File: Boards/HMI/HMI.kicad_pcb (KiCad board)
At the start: 2 copper layers, 250 x 150 mm, 177 parts, among them IC1 ISO1042BDWVR, IC6 MCP2515-e_ST, J1 1987724, J10 5442251, J11 5442251, J12 5442251, J13 5442251, J14 5442251, J15 5442251, J16 5442251, J17 5442251, J18 5442251, J19 5442251, J2 1987724, J20 5442251, J21 5442251, J22 5442251, J23 5442251, J24 5442251, J25 5442251, J26 5442251, J27 5442251, J28 5442251, J29 5442251, J3 5442251, J30 5442251, J31 5442251, J32 5442251, J33 5442251, J34 5442251, J35 5442251, J36 5442251, J37 5442251, J38 5442251, J39 5442251, J4 5442251, J40 5442251, J41 5442251, J42 5442251, J43 5442251, J44 5442251, J45 5442251, J46 5442251, J47 5442251, J48 5442251, J49 5442251, J5 5442251, J50 5442251, J51 5442251, J52 5442251, J53 5442251, J54 5442251, J55 5442251, J56 5442251, J57 5442251, J58 5442251, J6 5442251, J7 5442251, J8 5442251, J9 5442251, Q1 SSM3K361R,LF, Q10 SSM3K361R,LF, Q11 SSM3K361R,LF, Q12 SSM3K361R,LF, Q13 SSM3K361R,LF, Q14 SSM3K361R,LF, Q15 SSM3K361R,LF, Q16 SSM3K361R,LF, Q17 SSM3K361R,LF, Q18 SSM3K361R,LF, Q19 SSM3K361R,LF, Q2 SSM3K361R,LF, Q20 SSM3K361R,LF, Q21 SSM3K361R,LF, Q22 SSM3K361R,LF, Q23 SSM3K361R,LF, Q24 SSM3K361R,LF, Q3 SSM3K361R,LF, Q4 SSM3K361R,LF, Q5 SSM3K361R,LF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

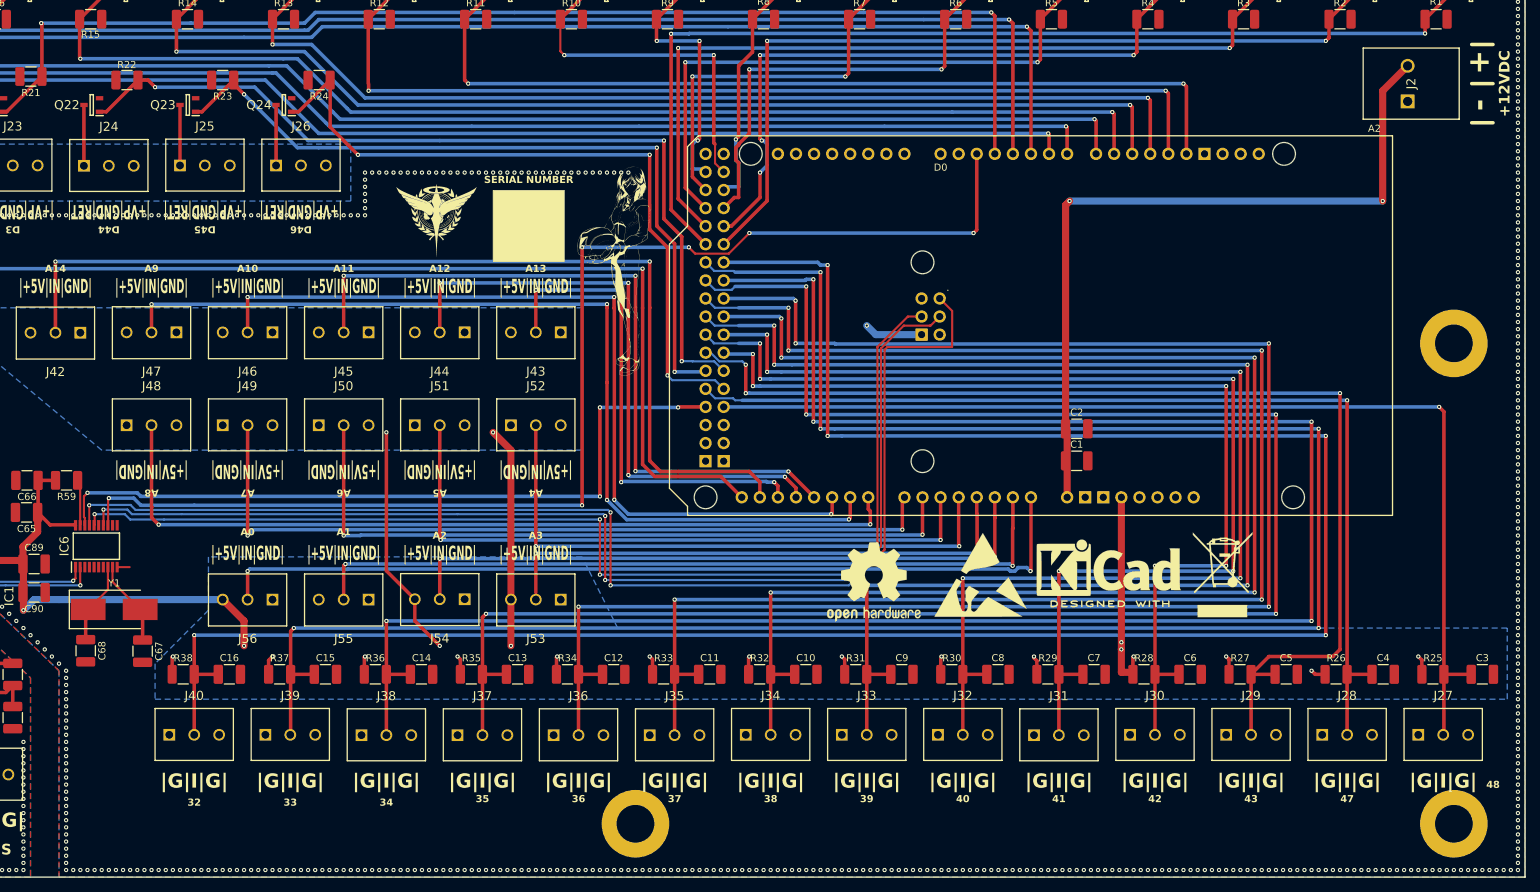
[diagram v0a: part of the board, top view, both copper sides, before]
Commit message: Update Gate Driver to use non NDA BS Chip
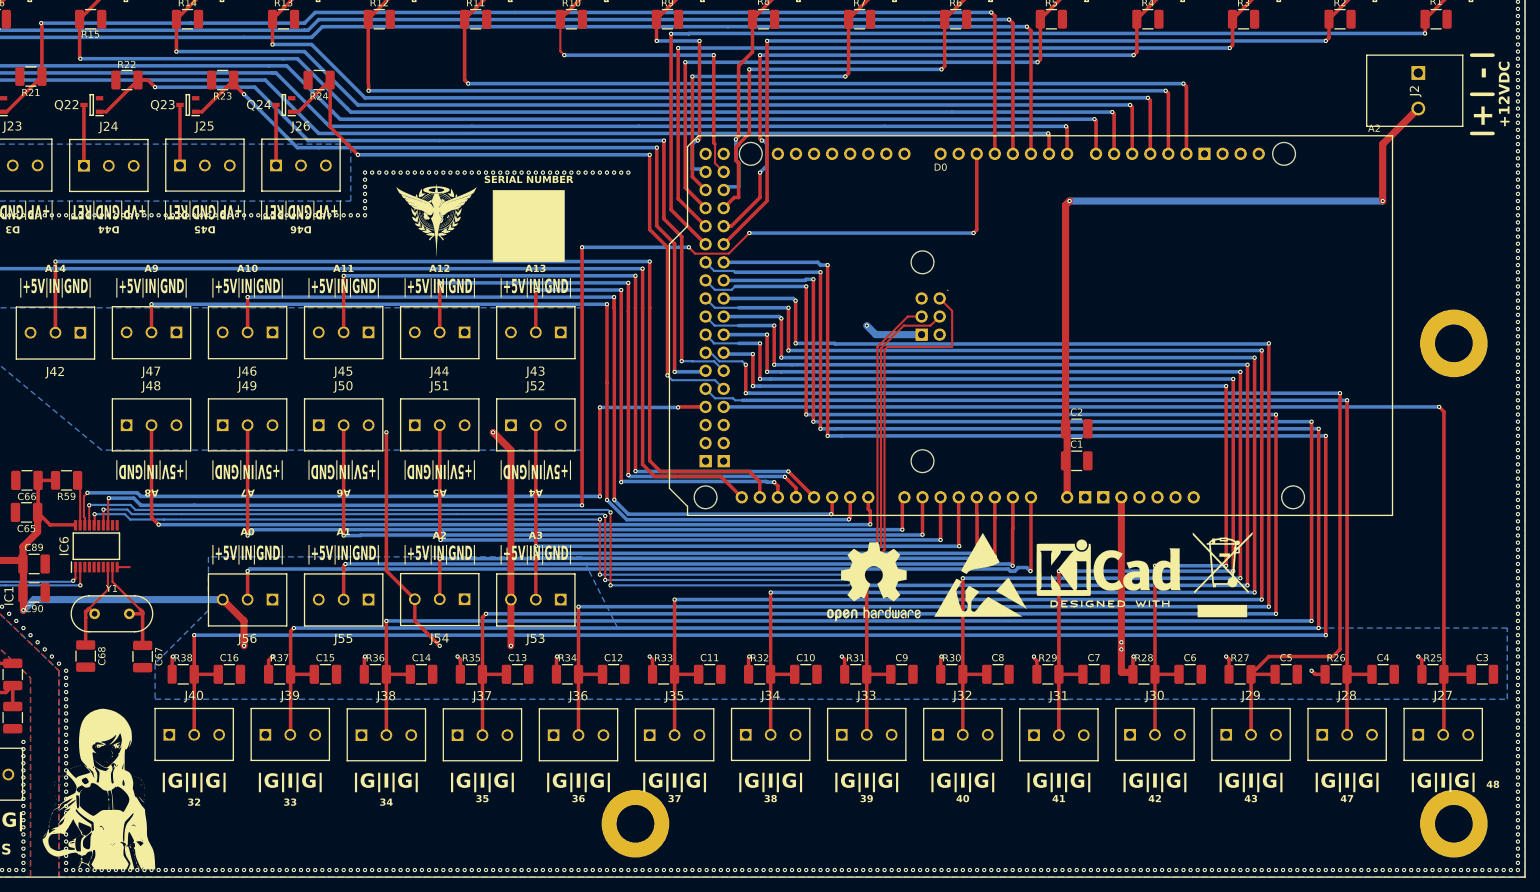
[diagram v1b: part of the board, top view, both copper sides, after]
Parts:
- removed the G*** at (148.5, 88.5)
- added G***: LOGO, InverterCom:Char_TieriaErde_20mm, F.Cu at (75.0, 162.0)
- Y1: footprint Crystal:Crystal_SMD_7050-2Pin_7.0x5.0mm_HandSoldering -> Crystal:Crystal_HC49-4H_Vertical
- moved J2 4.27 mm to (260.0, 62.0), turned to -90 degrees
- moved Y1 2.82 mm to (74.0, 138.0)
- moved C67 0.75 mm to (80.8, 144.0)
- moved C68 0.75 mm to (72.8, 143.9)
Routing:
- net +12V: track 106.4 -> 101.0 mm
- net Net-(IC6-OSC2): track 11.5 -> 13.5 mm
- net Net-(IC6-OSC1): track 12.0 -> 13.9 mm

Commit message: Update Layouts
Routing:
- net GND: vias 786 -> 985
- added copper zone on In1.Cu, net CANBUS_ISO_GND
- added copper zone on In2.Cu, net CANBUS_ISO_GND
- added copper zone on In1.Cu, net GND
- added copper zone on In2.Cu, net GND
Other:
- copper layers 2 -> 4
